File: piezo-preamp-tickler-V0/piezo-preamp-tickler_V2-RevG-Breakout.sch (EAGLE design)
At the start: 73 parts, among them IC1 OPA2134UA, J1 12V, J10 Buf2_BYPASS, J11 AUDIO-JACK3LGPADS, J12 AUDIO-JACK3LGPADS, J14 Battery, J2 12V, J3 Piezo, J4 12V, J5 Buf1_OUT, J6 OpAmp_IN, J7 12V, J8 OpAmp_OUT, J9 Buf2_IN, Q1 J201, Q2 J201SOT-23, Q3 DMN2400, Q4 BQ21040, Q5 SC4503, Q6 BQ297X, SW1 SWITCH_DPDT, SW2 INPUT-select, SW3 SPDT

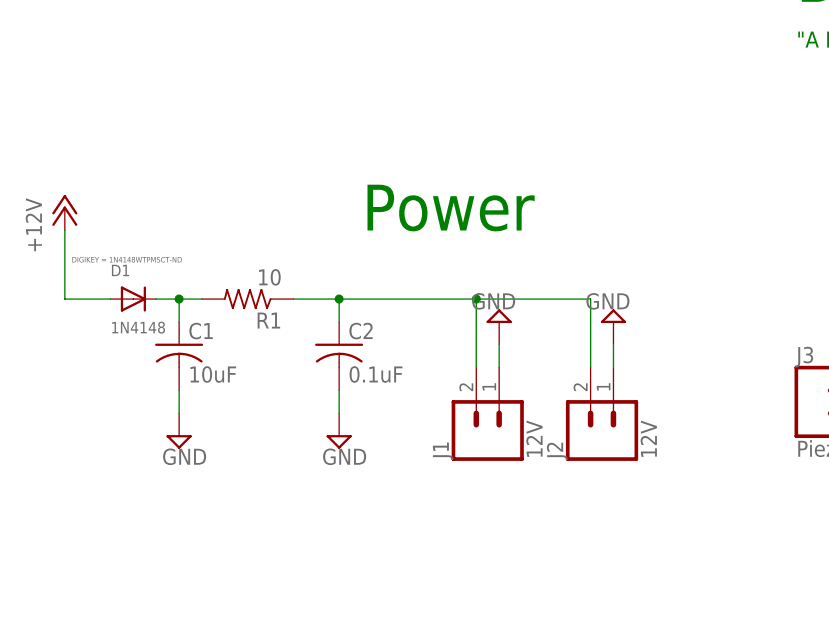
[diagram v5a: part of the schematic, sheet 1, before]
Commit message: new piezo preamp designs
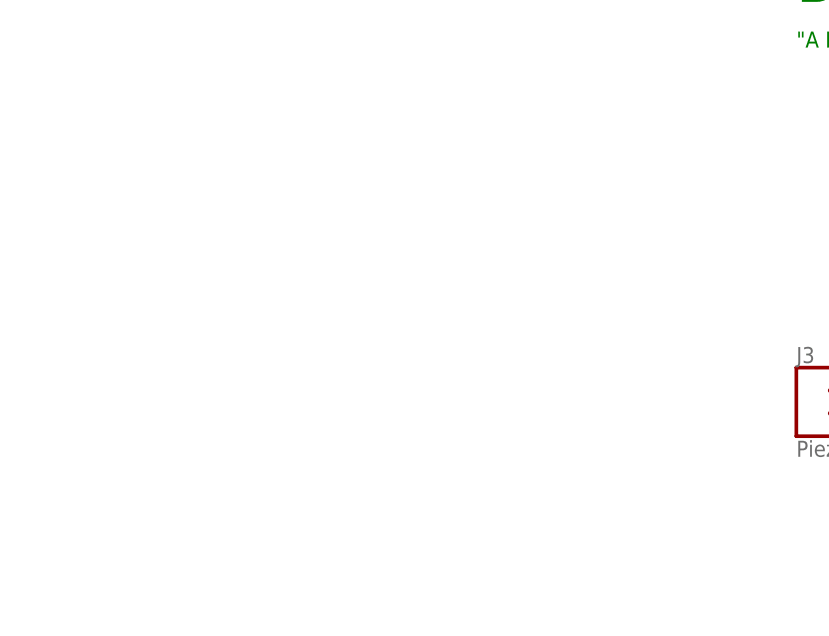
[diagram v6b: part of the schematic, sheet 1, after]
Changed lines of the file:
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@@
 <text x="-101.6" y="76.2" size="1.778" layer="91">"A Discrete FET Guitar Preamp" by J. Donald Tillman</text>
 <text x="167.64" y="53.34" size="1.778" layer="91">"Simple JFET Preamp for an iDevice Guitar Interface"</text>
-<wire x1="-114.3" y1="63.5" x2="-187.96" y2="63.5" width="0.1524" layer="98"/>
-<wire x1="-187.96" y1="63.5" x2="-187.96" y2="27.94" width="0.1524" layer="98"/>
-<wire x1="-187.96" y1="27.94" x2="-114.3" y2="27.94" width="0.1524" layer="98"/>
-<wire x1="-114.3" y1="27.94" x2="-114.3" y2="63.5" width="0.1524" layer="98"/>
-<text x="-149.86" y="55.88" size="5.08" layer="91">Power</text>
 </plain>
 <instances>
@@
 <attribute name="VALUE" x="272.542" y="32.512" size="1.778" layer="96"/>
 </instance>
-<instance part="C2" gate="G$1" x="-152.4" y="43.18"/>
 <instance part="C7" gate="G$1" x="91.44" y="30.48" rot="R90"/>
 <instance part="C5" gate="G$1" x="53.34" y="48.26"/>
 <instance part="R4" gate="G$1" x="-60.96" y="27.94" rot="R90"/>
 <instance part="C4" gate="G$1" x="-33.02" y="43.18" rot="R90"/>
-<instance part="P+1" gate="1" x="-182.88" y="58.42"/>
-<instance part="D1" gate="G$1" x="-175.26" y="48.26">
-<attribute name="DIGIKEY" x="-182.118" y="52.324" size="0.6096" layer="96" display="both"/>
-</instance>
 <instance part="Q2" gate="G$1" x="200.66" y="33.02"/>
 <instance part="TM1" gate="G$1" x="20.32" y="22.86"/>
-<instance part="R1" gate="G$1" x="-162.56" y="48.26" rot="R180"/>
 <instance part="R3" gate="G$1" x="-60.96" y="55.88" rot="R90"/>
 <instance part="R6" gate="G$1" x="20.32" y="48.26" rot="R90"/>
-<instance part="SUPPLY2" gate="GND" x="-152.4" y="33.02"/>
 <instance part="Q1" gate="G$1" x="-63.5" y="40.64"/>
 <instance part="C3" gate="G$1" x="-50.8" y="27.94"/>
-<instance part="C1" gate="G$1" x="-170.18" y="43.18"/>
-<instance part="SUPPLY1" gate="GND" x="-170.18" y="33.02"/>
 <instance part="R13" gate="G$1" x="137.16" y="10.16" rot="R90"/>
 <instance part="R2" gate="G$1" x="-81.28" y="30.48" rot="R90"/>
@@
 <instance part="C6" gate="G$1" x="81.28" y="10.16" rot="R90"/>
 <instance part="R12" gate="G$1" x="68.58" y="10.16" rot="MR180"/>
-<instance part="J1" gate="G$1" x="-134.62" y="33.02" rot="R90"/>
-<instance part="J2" gate="G$1" x="-121.92" y="33.02" rot="R90"/>
-<instance part="SUPPLY4" gate="GND" x="-121.92" y="45.72" rot="R180"/>
 <instance part="D3" gate="G$1" x="-73.66" y="25.4" rot="R270"/>
-<instance part="SUPPLY3" gate="GND" x="-134.62" y="45.72" rot="R180"/>
 <instance part="J4" gate="G$1" x="-15.24" y="83.82" rot="R180"/>
 <instance part="J7" gate="G$1" x="76.2" y="78.74" rot="R180"/>
@@
 </busses>
 <nets>
-<net name="GND" class="0">
-<segment>
-<pinref part="C2" gate="G$1" pin="2"/>
-<pinref part="SUPPLY2" gate="GND" pin="GND"/>
-<wire x1="-152.4" y1="38.1" x2="-152.4" y2="35.56" width="0.1524" layer="91"/>
-</segment>
-<segment>
-<pinref part="C1" gate="G$1" pin="2"/>
-<pinref part="SUPPLY1" gate="GND" pin="GND"/>
-<wire x1="-170.18" y1="38.1" x2="-170.18" y2="35.56" width="0.1524" layer="91"/>
-</segment>
-<segment>
-<pinref part="SUPPLY4" gate="GND" pin="GND"/>
-<pinref part="J2" gate="G$1" pin="1"/>
-<wire x1="-121.92" y1="43.18" x2="-121.92" y2="40.64" width="0.1524" layer="91"/>
-</segment>
-<segment>
-<pinref part="SUPPLY3" gate="GND" pin="GND"/>
-<pinref part="J1" gate="G$1" pin="1"/>
-<wire x1="-134.62" y1="43.18" x2="-134.62" y2="40.64" width="0.1524" layer="91"/>
-</segment>
-</net>
 <net name="N$1" class="0">
 <segment>
@@
 </segment>
 </net>
-<net name="+12V" class="0">
-<segment>
-<pinref part="P+1" gate="1" pin="+12V"/>
-<pinref part="D1" gate="G$1" pin="A"/>
-<wire x1="-182.88" y1="55.88" x2="-182.88" y2="48.26" width="0.1524" layer="91"/>
-<wire x1="-182.88" y1="48.26" x2="-177.8" y2="48.26" width="0.1524" layer="91"/>
-</segment>
-</net>
-<net name="N$16" class="0">
-<segment>
-<pinref part="D1" gate="G$1" pin="C"/>
-<pinref part="R1" gate="G$1" pin="2"/>
-<wire x1="-172.72" y1="48.26" x2="-170.18" y2="48.26" width="0.1524" layer="91"/>
-<pinref part="C1" gate="G$1" pin="1"/>
-<wire x1="-170.18" y1="48.26" x2="-167.64" y2="48.26" width="0.1524" layer="91"/>
-<wire x1="-170.18" y1="45.72" x2="-170.18" y2="48.26" width="0.1524" layer="91"/>
-<junction x="-170.18" y="48.26"/>
-</segment>
-</net>
 <net name="N$25" class="0">
 <segment>
@@
 <wire x1="30.48" y1="76.2" x2="30.48" y2="68.58" width="0.1524" layer="91"/>
 <junction x="30.48" y="68.58"/>
-</segment>
-</net>
-<net name="N$43" class="0">
-<segment>
-<pinref part="J2" gate="G$1" pin="2"/>
-<wire x1="-124.46" y1="48.26" x2="-124.46" y2="40.64" width="0.1524" layer="91"/>
-<pinref part="J1" gate="G$1" pin="2"/>
-<wire x1="-137.16" y1="48.26" x2="-137.16" y2="40.64" width="0.1524" layer="91"/>
-<wire x1="-137.16" y1="48.26" x2="-124.46" y2="48.26" width="0.1524" layer="91"/>
-<junction x="-137.16" y="48.26"/>
-<pinref part="C2" gate="G$1" pin="1"/>
-<wire x1="-152.4" y1="48.26" x2="-152.4" y2="45.72" width="0.1524" layer="91"/>
-<wire x1="-152.4" y1="48.26" x2="-137.16" y2="48.26" width="0.1524" layer="91"/>
-<junction x="-152.4" y="48.26"/>
-<pinref part="R1" gate="G$1" pin="1"/>
-<wire x1="-157.48" y1="48.26" x2="-152.4" y2="48.26" width="0.1524" layer="91"/>
 </segment>
 </net>
@@
 <text x="139.7" y="185.42" size="1.778" layer="91">Battery Charging</text>
 <text x="182.88" y="81.28" size="1.778" layer="91">Power LED</text>
+<wire x1="121.92" y1="238.76" x2="48.26" y2="238.76" width="0.1524" layer="98"/>
+<wire x1="48.26" y1="238.76" x2="48.26" y2="203.2" width="0.1524" layer="98"/>
+<wire x1="48.26" y1="203.2" x2="121.92" y2="203.2" width="0.1524" layer="98"/>
+<wire x1="121.92" y1="203.2" x2="121.92" y2="238.76" width="0.1524" layer="98"/>
+<text x="86.36" y="231.14" size="5.08" layer="91">Power</text>
 </plain>
 <instances>
@@
 <instance part="Q5" gate="G$1" x="109.22" y="50.8" rot="MR0"/>
 <instance part="L1" gate="G$1" x="109.22" y="66.04" rot="R90"/>
+<instance part="C2" gate="G$1" x="83.82" y="218.44"/>
+<instance part="P+1" gate="1" x="53.34" y="233.68"/>
+<instance part="D1" gate="G$1" x="60.96" y="223.52">
+<attribute name="DIGIKEY" x="54.102" y="227.584" size="0.6096" layer="96" display="both"/>
+</instance>
+<instance part="R1" gate="G$1" x="73.66" y="223.52" rot="R180"/>
+<instance part="SUPPLY2" gate="GND" x="83.82" y="208.28"/>
+<instance part="C1" gate="G$1" x="66.04" y="218.44"/>
+<instance part="SUPPLY1" gate="GND" x="66.04" y="208.28"/>
+<instance part="J1" gate="G$1" x="101.6" y="208.28" rot="R90"/>
+<instance part="J2" gate="G$1" x="114.3" y="208.28" rot="R90"/>
+<instance part="SUPPLY4" gate="GND" x="114.3" y="220.98" rot="R180"/>
+<instance part="SUPPLY3" gate="GND" x="101.6" y="220.98" rot="R180"/>
 </instances>
 <busses>
@@
 <pinref part="Q5" gate="G$1" pin="GND"/>
 <wire x1="129.54" y1="50.8" x2="124.46" y2="50.8" width="0.1524" layer="91"/>
+</segment>
+<segment>
+<pinref part="C2" gate="G$1" pin="2"/>
+<pinref part="SUPPLY2" gate="GND" pin="GND"/>
+<wire x1="83.82" y1="213.36" x2="83.82" y2="210.82" width="0.1524" layer="91"/>
+</segment>
+<segment>
+<pinref part="C1" gate="G$1" pin="2"/>
+<pinref part="SUPPLY1" gate="GND" pin="GND"/>
+<wire x1="66.04" y1="213.36" x2="66.04" y2="210.82" width="0.1524" layer="91"/>
+</segment>
+<segment>
+<pinref part="SUPPLY4" gate="GND" pin="GND"/>
+<pinref part="J2" gate="G$1" pin="1"/>
+<wire x1="114.3" y1="218.44" x2="114.3" y2="215.9" width="0.1524" layer="91"/>
+</segment>
+<segment>
+<pinref part="SUPPLY3" gate="GND" pin="GND"/>
+<pinref part="J1" gate="G$1" pin="1"/>
+<wire x1="101.6" y1="218.44" x2="101.6" y2="215.9" width="0.1524" layer="91"/>
 </segment>
 </net>
@@
 <pinref part="C12" gate="G$1" pin="1"/>
 <pinref part="C13" gate="G$1" pin="1"/>
+</segment>
+<segment>
+<pinref part="P+1" gate="1" pin="+12V"/>
+<pinref part="D1" gate="G$1" pin="A"/>
+<wire x1="53.34" y1="231.14" x2="53.34" y2="223.52" width="0.1524" layer="91"/>
+<wire x1="53.34" y1="223.52" x2="58.42" y2="223.52" width="0.1524" layer="91"/>
 </segment>
 </net>
@@
 </segment>
 </net>
+<net name="N$16" class="0">
+<segment>
+<pinref part="D1" gate="G$1" pin="C"/>
+<pinref part="R1" gate="G$1" pin="2"/>
+<wire x1="63.5" y1="223.52" x2="66.04" y2="223.52" width="0.1524" layer="91"/>
+<pinref part="C1" gate="G$1" pin="1"/>
+<wire x1="66.04" y1="223.52" x2="68.58" y2="223.52" width="0.1524" layer="91"/>
+<wire x1="66.04" y1="220.98" x2="66.04" y2="223.52" width="0.1524" layer="91"/>
+<junction x="66.04" y="223.52"/>
+</segment>
+</net>
+<net name="N$43" class="0">
+<segment>
+<pinref part="J2" gate="G$1" pin="2"/>
+<wire x1="111.76" y1="223.52" x2="111.76" y2="215.9" width="0.1524" layer="91"/>
+<pinref part="J1" gate="G$1" pin="2"/>
+<wire x1="99.06" y1="223.52" x2="99.06" y2="215.9" width="0.1524" layer="91"/>
+<wire x1="99.06" y1="223.52" x2="111.76" y2="223.52" width="0.1524" layer="91"/>
+<junction x="99.06" y="223.52"/>
+<pinref part="C2" gate="G$1" pin="1"/>
+<wire x1="83.82" y1="223.52" x2="83.82" y2="220.98" width="0.1524" layer="91"/>
+<wire x1="83.82" y1="223.52" x2="99.06" y2="223.52" width="0.1524" layer="91"/>
+<junction x="83.82" y="223.52"/>
+<pinref part="R1" gate="G$1" pin="1"/>
+<wire x1="78.74" y1="223.52" x2="83.82" y2="223.52" width="0.1524" layer="91"/>
+</segment>
+</net>

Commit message: piezo preamp updates
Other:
- moved on the sheet: C1, C11, C12, C13, C2, C9, D1, D6, J1, J2, L1, LED2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
